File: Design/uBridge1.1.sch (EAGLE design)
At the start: 42 parts, among them J1 22-27-2051-05, J2 22-27-2051-05, U1 A4950, U2 ACS723, U3 A4950, U4 ACS723

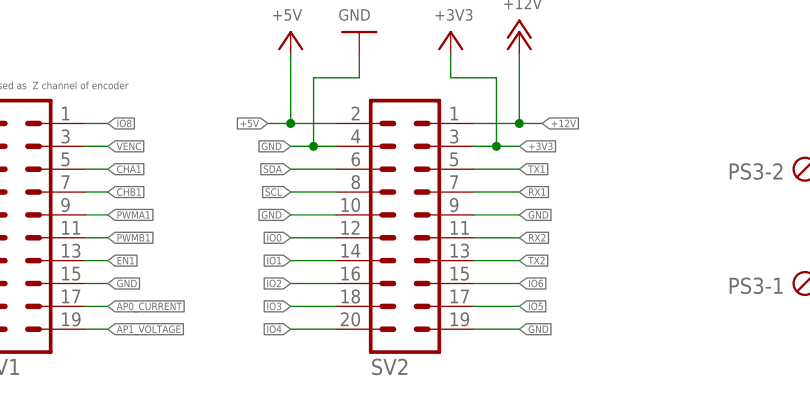
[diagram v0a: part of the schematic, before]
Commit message: Solved little issue on label name and release file name.
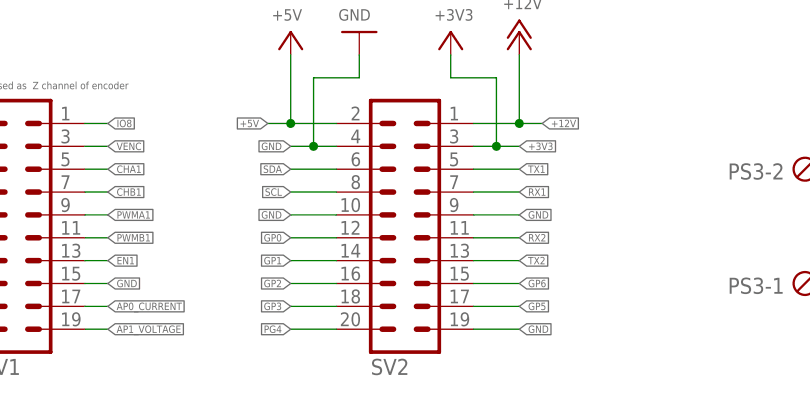
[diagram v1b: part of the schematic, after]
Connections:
- net IO0 renamed GP0
- net IO1 renamed GP1
- net IO2 renamed GP2
- net IO3 renamed GP3
- net IO4 renamed PG4
- net IO5 renamed GP5
- net IO6 renamed GP6
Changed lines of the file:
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@@
 </segment>
 </net>
-<net name="IO4" class="0">
+<net name="PG4" class="0">
 <segment>
 <wire x1="60.96" y1="10.16" x2="55.88" y2="10.16" width="0.1524" layer="91"/>
@@
 </segment>
 </net>
-<net name="IO3" class="0">
+<net name="GP3" class="0">
 <segment>
 <label x="55.88" y="12.7" size="0.8128" layer="95" font="vector" rot="MR0" xref="yes"/>
@@
 </segment>
 </net>
-<net name="IO2" class="0">
+<net name="GP2" class="0">
 <segment>
 <wire x1="60.96" y1="15.24" x2="55.88" y2="15.24" width="0.1524" layer="91"/>
@@
 </segment>
 </net>
-<net name="IO1" class="0">
+<net name="GP1" class="0">
 <segment>
 <wire x1="60.96" y1="17.78" x2="55.88" y2="17.78" width="0.1524" layer="91"/>
@@
 </segment>
 </net>
-<net name="IO5" class="0">
+<net name="GP5" class="0">
 <segment>
 <wire x1="76.2" y1="12.7" x2="81.28" y2="12.7" width="0.1524" layer="91"/>
@@
 </segment>
 </net>
-<net name="IO6" class="0">
+<net name="GP6" class="0">
 <segment>
 <wire x1="76.2" y1="15.24" x2="81.28" y2="15.24" width="0.1524" layer="91"/>
@@
 </segment>
 </net>
-<net name="IO0" class="0">
+<net name="GP0" class="0">
 <segment>
 <wire x1="60.96" y1="20.32" x2="55.88" y2="20.32" width="0.1524" layer="91"/>
